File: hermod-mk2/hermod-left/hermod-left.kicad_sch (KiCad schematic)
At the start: 41 parts, among them J1 USB_C_Receptacle_USB2.0, J2 Conn_01x05, J3 USB_C_Receptacle_USB2.0, Q1 AO3401A, Q2 MMUN2233LT1G, U2 PRTR5V0U2X, U3 XC6206PxxxMR-Regulator_Linear, U4 CR2013-MI2120, U5 TXB0101, U8 STM32G474RETx

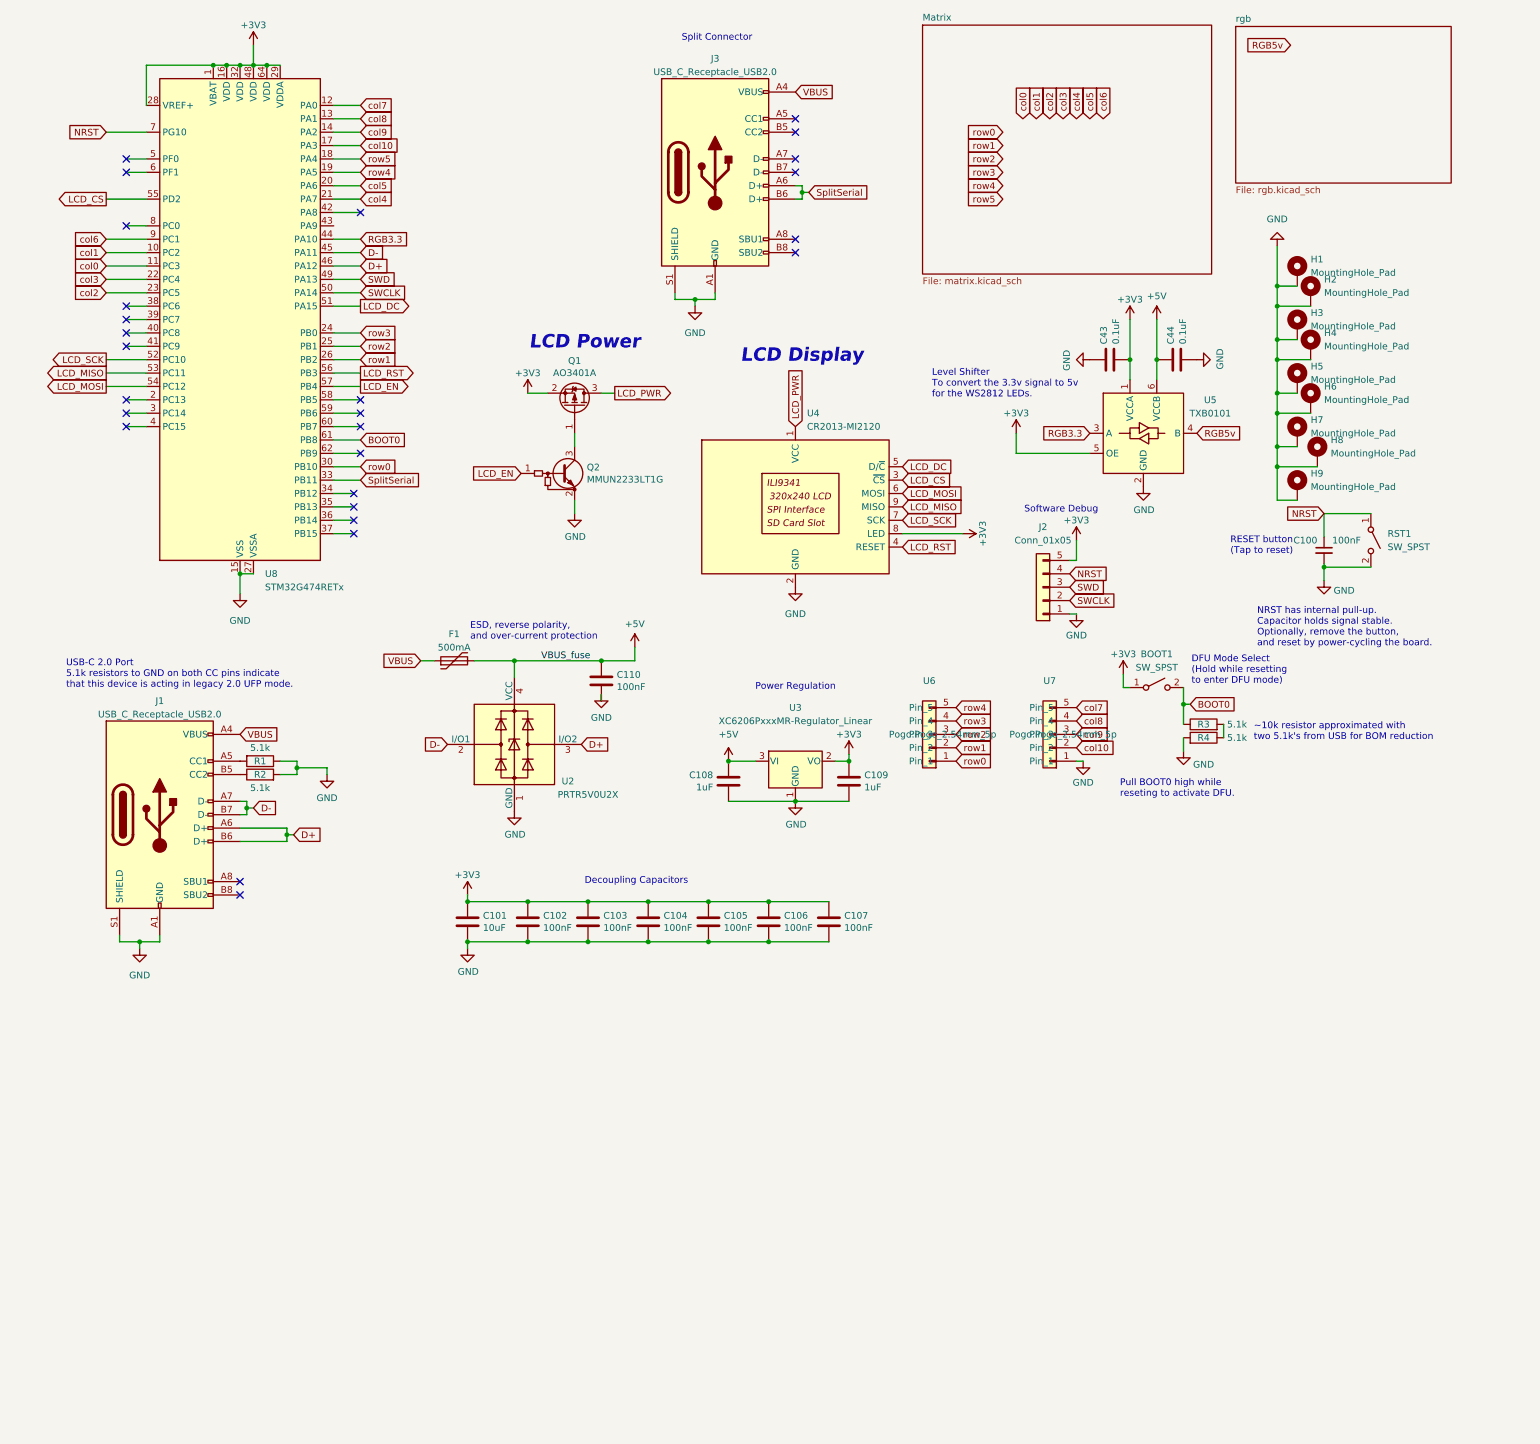
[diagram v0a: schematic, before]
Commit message: Fixed up the 5v for LEDs
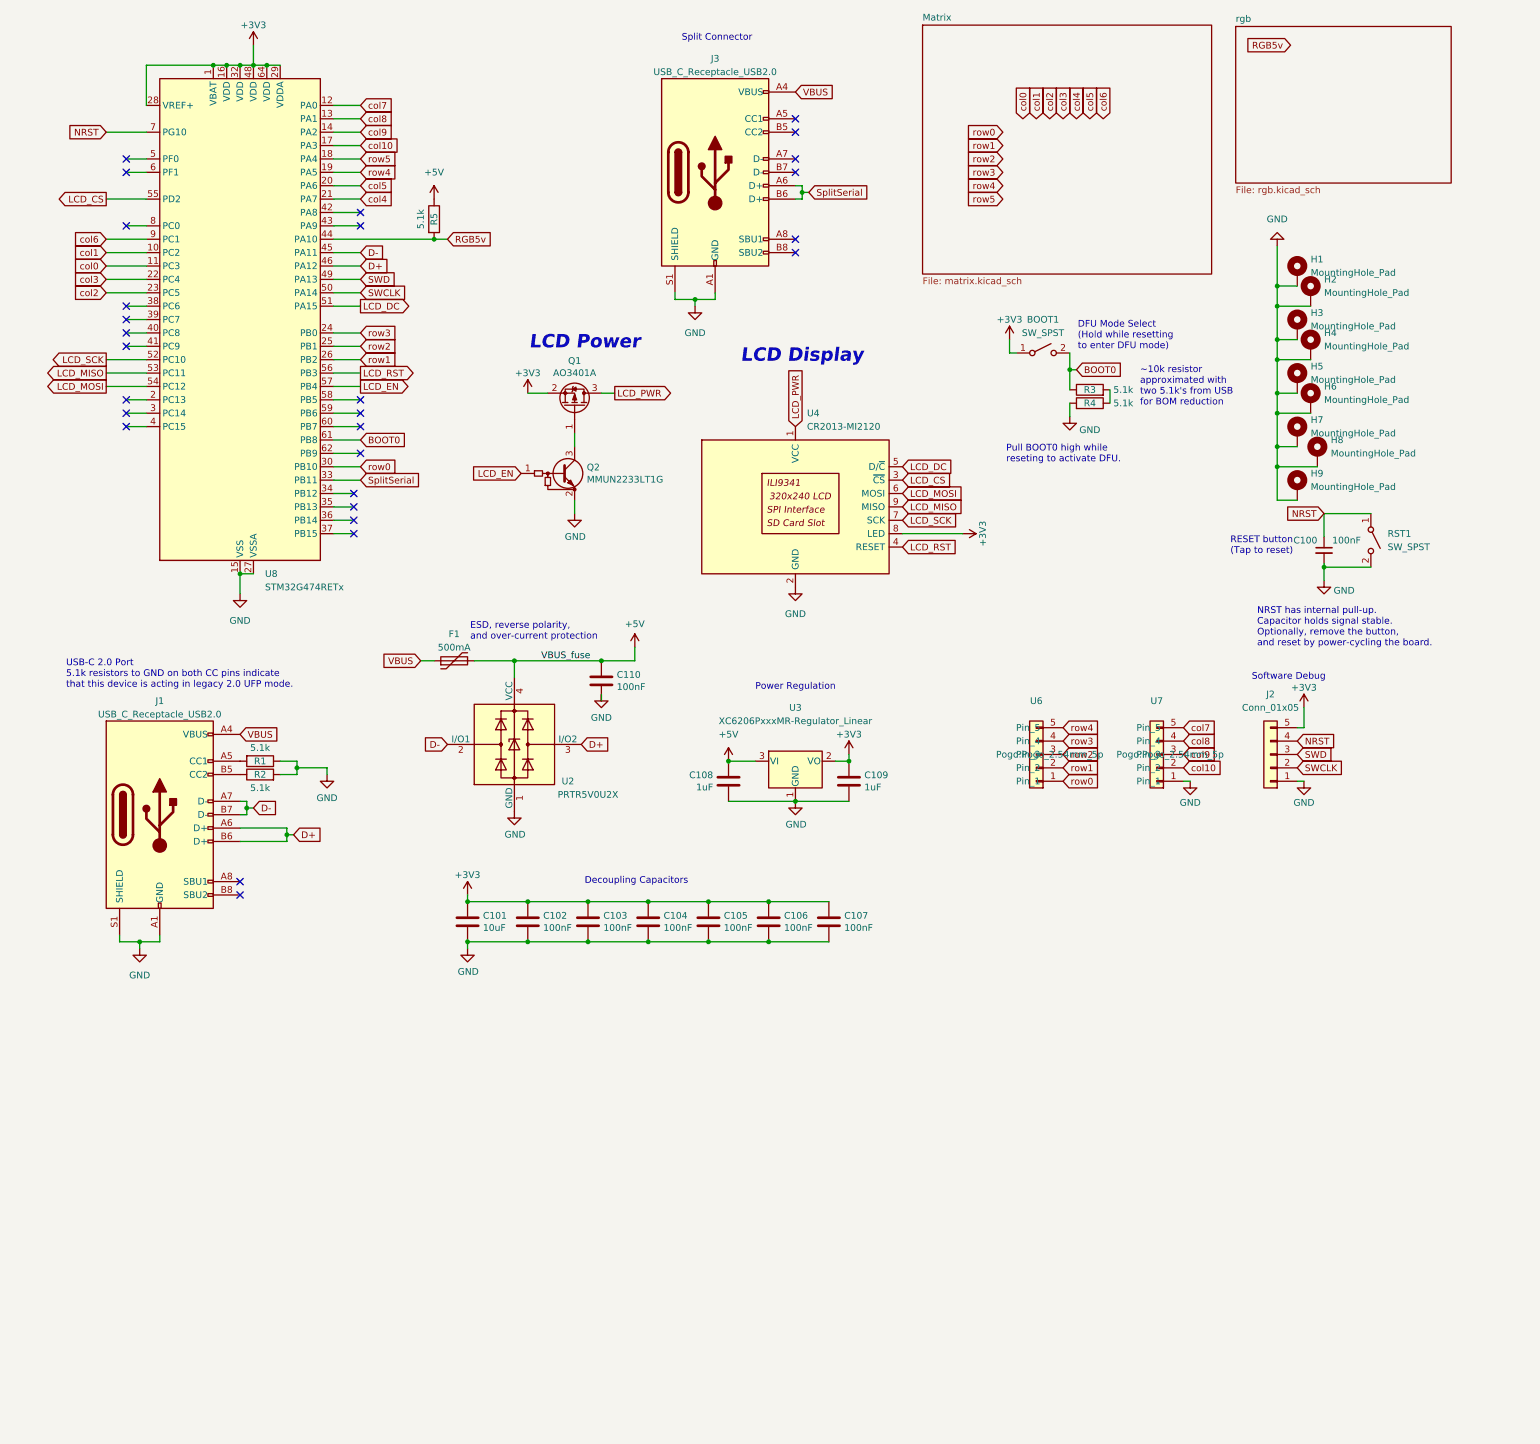
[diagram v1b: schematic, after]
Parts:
- removed C43, C44: 0.1uF, Capacitor_SMD:C_0402_1005Metric, symbol Device:C
- removed U5: TXB0101, Package_TO_SOT_SMD:SOT-363_SC-70-6_Handsoldering, symbol PCM_marbastlib-various:TXB0101
- added R5: 5.1k, Resistor_SMD:R_0402_1005Metric, symbol Device:R
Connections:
- net RGB3.3 is gone; now on net RGB5v: U8.44 (PA10)
- net +5V: now also R5.1
- net RGB5v: now also R5.2
- no-connect marks 27 -> 28
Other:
- note removed: "Level Shifter To convert the 3.3v signal to 5v for the WS2812 LEDs."
- moved on the sheet: BOOT1, J2, R3, R4, U6, U7

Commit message: Fixed up hermod mk1 and updated hermod mk2
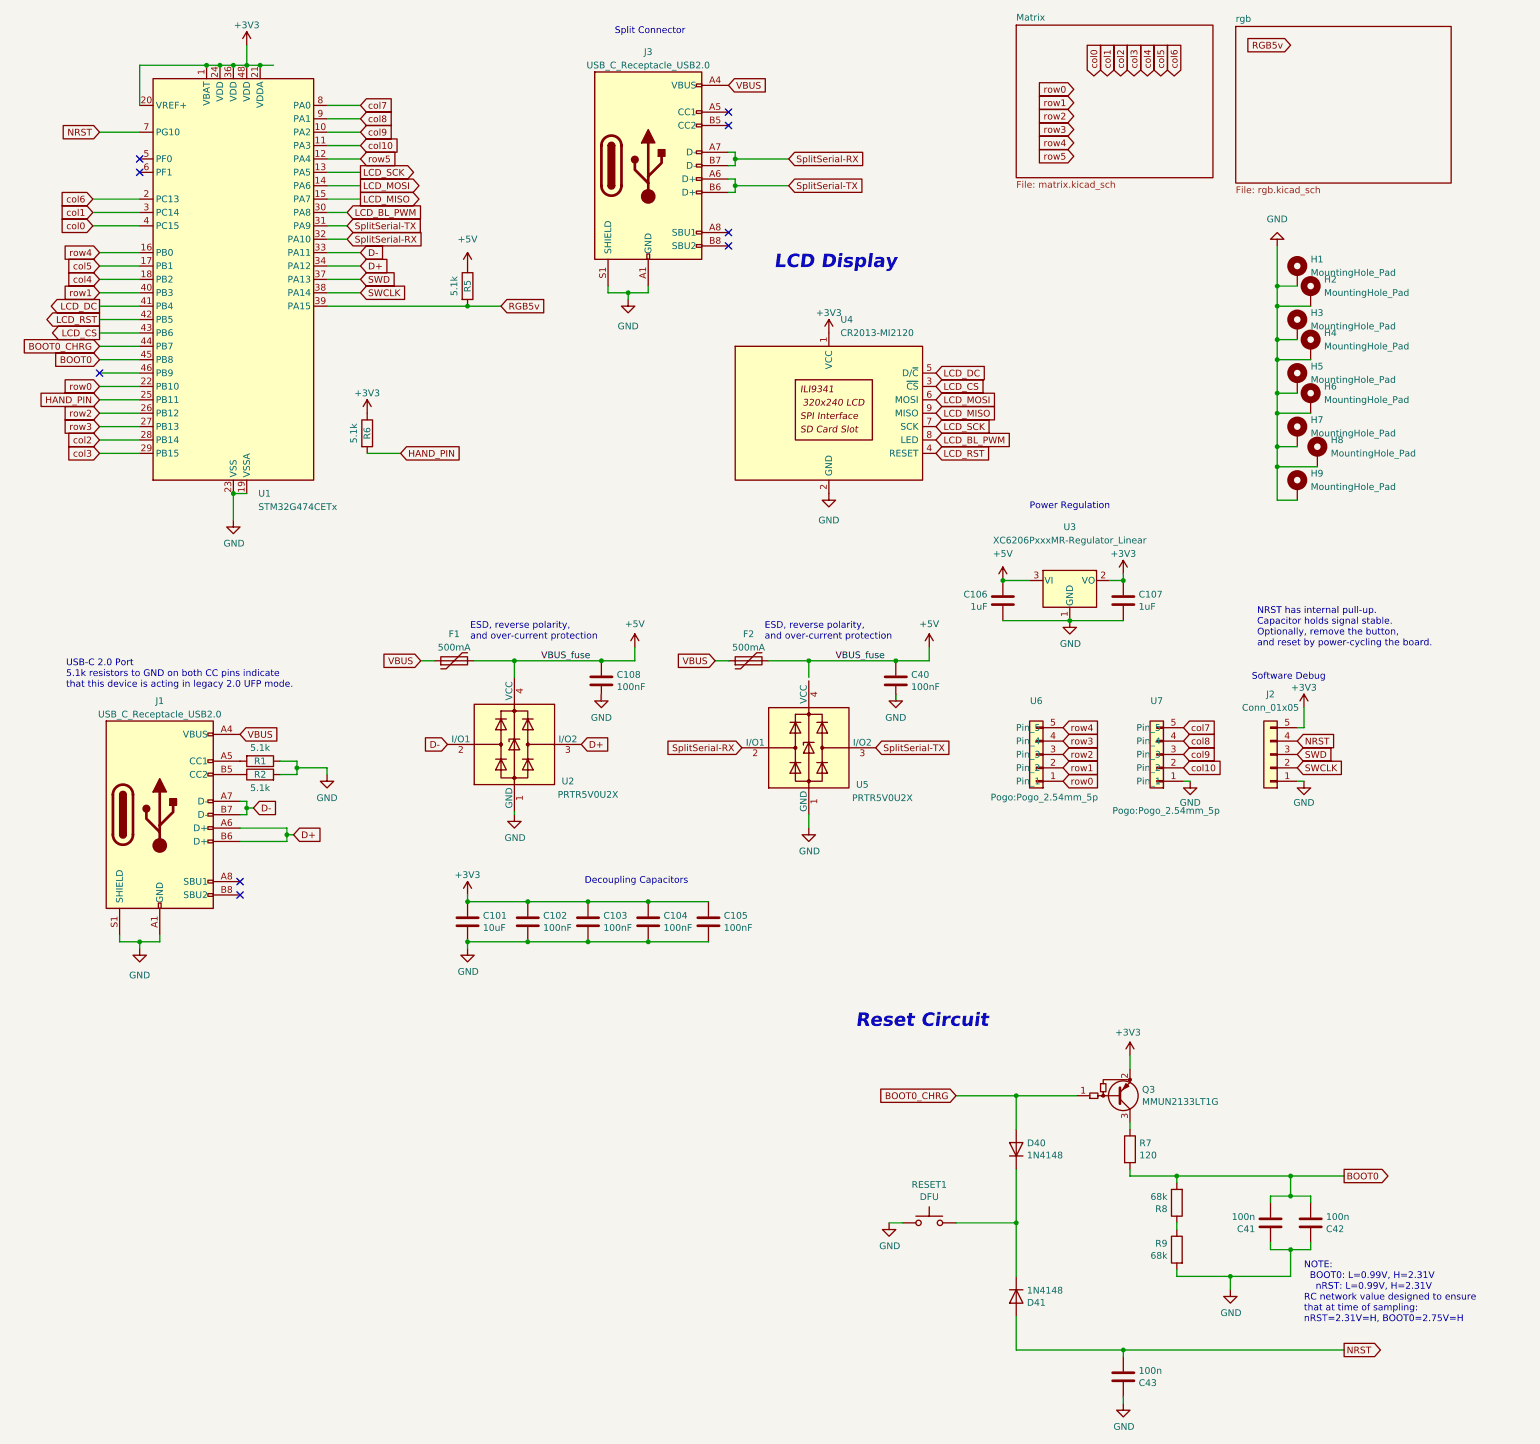
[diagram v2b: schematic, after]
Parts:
- removed BOOT1, RST1: SW_SPST, Button_Switch_SMD:SW_SPST_TL3342, symbol Switch:SW_SPST
- removed C100: 100nF, Capacitor_SMD:C_0402_1005Metric, symbol Device:C_Small
- removed C106, C107: 100nF, Capacitor_SMD:C_0402_1005Metric, symbol Device:C
- removed Q1: AO3401A, Package_TO_SOT_SMD:SOT-23-3, symbol Transistor_FET:AO3401A
- removed Q2: MMUN2233LT1G, Package_TO_SOT_SMD:SOT-23-3, symbol Device:Q_NPN_BEC_BRT
- removed R3, R4: 5.1k, Resistor_SMD:R_0402_1005Metric, symbol Device:R
- removed U8: STM32G474RETx, Package_QFP:LQFP-64_10x10mm_P0.5mm, symbol MCU_ST_STM32G4:STM32G474RETx
- added C40: 100nF, Capacitor_SMD:C_0402_1005Metric, symbol Device:C
- added C41, C42, C43: 100n, Capacitor_SMD:C_0805_2012Metric, symbol Device:C
- added D40, D41: 1N4148, Diode_SMD:D_SOD-123, symbol Device:D
- added F2: 500mA, Fuse:Fuse_1206_3216Metric, symbol Device:Polyfuse
- added Q3: MMUN2133LT1G, Package_TO_SOT_SMD:SOT-23-3, symbol Device:Q_PNP_BEC_BRT
- added R6: 5.1k, Resistor_SMD:R_0402_1005Metric, symbol Device:R
- added R7: 120, Resistor_SMD:R_0805_2012Metric, symbol Device:R
- added R8, R9: 68k, Resistor_SMD:R_0805_2012Metric, symbol Device:R
- added RESET1: DFU, Button_Switch_SMD:SW_SPST_TL3342, symbol Switch:SW_Push
- added U1: STM32G474CETx, Package_QFP:LQFP-48_7x7mm_P0.5mm, symbol MCU_ST_STM32G4:STM32G474CETx
- added U5: PRTR5V0U2X, Package_TO_SOT_SMD:SOT-143, symbol Power_Protection:PRTR5V0U2X
- renumbered C108 to C106, C109 to C107, C110 to C108
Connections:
- net LCD_PWR is gone; now on net +3V3: U4.1 (VCC)
- net +3V3: now also Q3.2 (E), R6.1, U1.1 (VBAT), U1.20 (VREF+), U1.21 (VDDA), U1.24 (VDD), U1.36 (VDD), U1.48 (VDD); no longer U4.8 (LED)
- net +5V: now also C40.1, F2.2
- net BOOT0: now also C41.2, C42.2, R7.2, R8.2, U1.45 (PB8)
- net D+: now also U1.34 (PA12)
- net D-: now also U1.33 (PA11)
- net GND: now also C40.2, C41.1, C42.1, C43.1, R9.2, RESET1.1, U1.19 (VSSA), U1.23 (VSS), U1.35 (VSS), U1.47 (VSS), U5.1 (GND)
- net LCD_CS: now also U1.43 (PB6)
- net LCD_DC: now also U1.41 (PB4)
- net LCD_MISO: now also U1.15 (PA7)
- net LCD_MOSI: now also U1.14 (PA6)
- net LCD_RST: now also U1.42 (PB5)
- net LCD_SCK: now also U1.13 (PA5)
- net NRST: now also C43.2, D41.2 (A), U1.7 (PG10)
- net RGB5v: now also U1.39 (PA15)
- net SWCLK: now also U1.38 (PA14)
- net SWD: now also U1.37 (PA13)
- net VBUS: now also F2.1
- net col0: now also U1.4 (PC15)
- net col1: now also U1.3 (PC14)
- net col10: now also U1.11 (PA3)
- net col2: now also U1.28 (PB14)
- net col3: now also U1.29 (PB15)
- net col4: now also U1.18 (PB2)
- net col5: now also U1.17 (PB1)
- net col6: now also U1.2 (PC13)
- net col7: now also U1.8 (PA0)
- net col8: now also U1.9 (PA1)
- net col9: now also U1.10 (PA2)
- net row0: now also U1.22 (PB10)
- net row1: now also U1.40 (PB3)
- net row2: now also U1.26 (PB12)
- net row3: now also U1.27 (PB13)
- net row4: now also U1.16 (PB0)
- net row5: now also U1.12 (PA4)
- net SplitSerial-RX: now reaches J3.A7 (D-)
- net SplitSerial-RX: now also J3.B7 (D-), U1.32 (PA10), U5.2 (I/O1)
- net SplitSerial renamed SplitSerial-TX
- net SplitSerial-TX: now also U1.31 (PA9), U5.3 (I/O2)
- new net: D40.1 (K), D41.1 (K), RESET1.2
- new net: Q3.3 (C), R7.1
- new net: R8.1, R9.1
- new net BOOT0_CHRG: D40.2 (A), Q3.1 (B), U1.44 (PB7)
- new net HAND_PIN: R6.2, U1.25 (PB11)
- new net LCD_BL_PWM: U1.30 (PA8), U4.8 (LED)
- no-connect marks 28 -> 9
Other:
- note added: "NOTE: BOOT0: L=0.99V, H=2.31V nRST: L=0.99V, H=2.31V RC network value designed to ensure that at time of sampling: nRST=2.31V=H, BOOT0=2.75V=H"
- note added: "Reset Circuit"
- note removed: "DFU Mode Select (Hold while resetting to enter DFU mode)"
- note removed: "LCD Power"
- note removed: "Pull BOOT0 high while reseting to activate DFU."
- note removed: "RESET button (Tap to reset)"
- note removed: "~10k resistor approximated with two 5.1k's from USB for BOM reduction"
- moved on the sheet: C106, C107, J3, U3, U4
